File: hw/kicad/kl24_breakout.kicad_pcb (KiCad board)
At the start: 2 copper layers, 36.1 x 20.8 mm, 65 parts, among them J1 USB-micro-ab, J2 ARM_10PIN, P1 BATT+, P10 TST, P11 TST, P12 TST, P13 TST, P14 TST, P15 TST, P16 TST, P17 TST, P18 TST, P19 TST, P2 BATT-, P20 TST, P21 TST, P22 TST, P23 TST, P24 TST, P25 TST, P26 TST, P27 TST, P28 TST, P29 TST, P3 TST, P30 TST, P31 TST, P32 TST, P33 TST, P34 TST, P35 BATT_BACKUP+, P36 BATT_BACKUP-, P37 USB_V, P38 USB_GND, P4 TST, P5 TST, P6 TST, P7 TST, P8 TST, P9 TST, U1 MCP73831, U2 M25P05-A, U3 MKL24Z64VFM4, U4 MCP1640_SOT23, U5 LP3985, X1 CRYSTAL

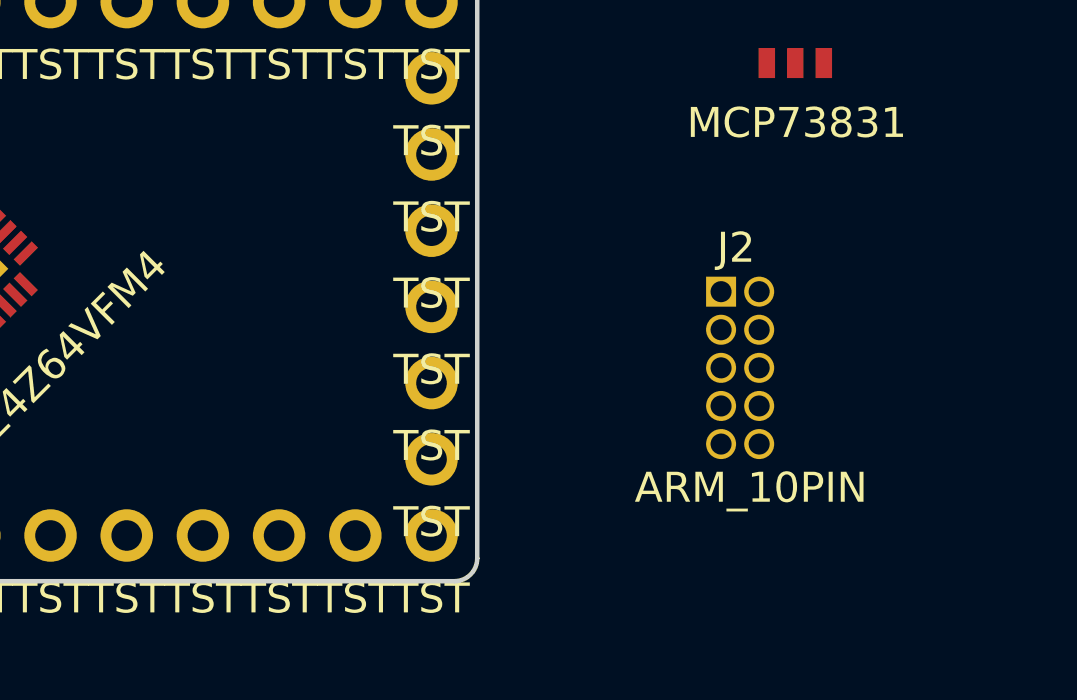
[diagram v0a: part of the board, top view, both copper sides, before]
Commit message: - switch arm 10pin header for smt version
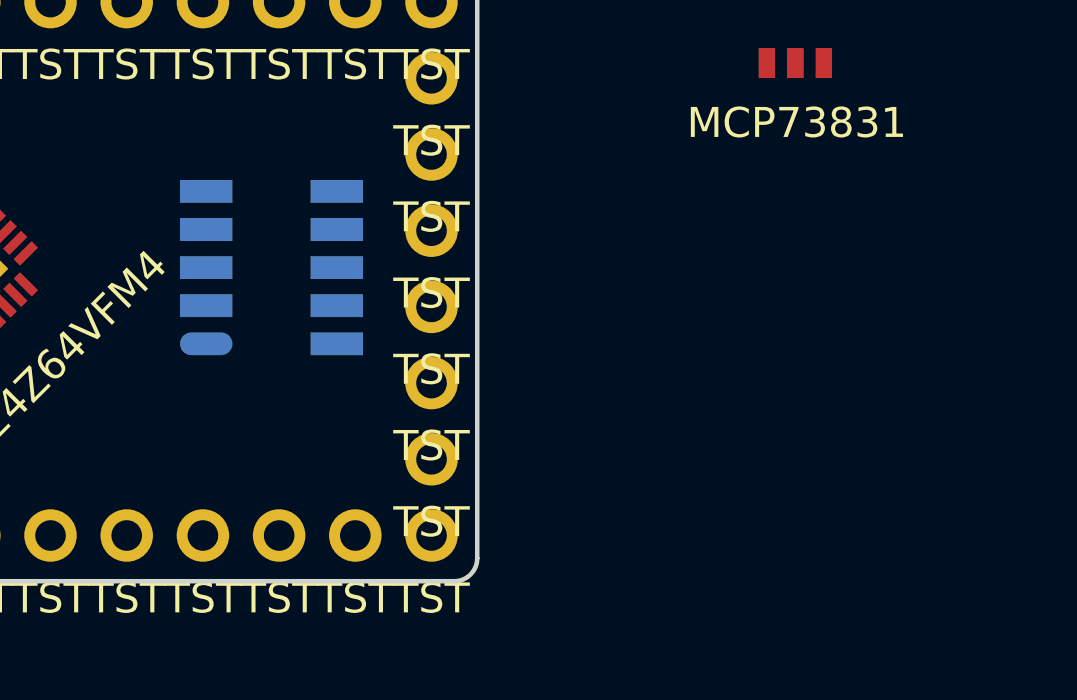
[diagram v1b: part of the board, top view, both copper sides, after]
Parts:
- J2: footprint ARM_10_PIN -> ARM_10_PIN_SMT; moved to B.Cu
- moved J2 15.3 mm to (139.4, 71.1), turned to 90 degrees
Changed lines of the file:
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@@
     (mod_text_size 1 1)
     (mod_text_width 0.15)
-    (pad_size 3.4 3.4)
-    (pad_drill 2)
+    (pad_size 0.76 1.75)
+    (pad_drill 0)
     (pad_to_mask_clearance 0)
     (aux_axis_origin 0 0)
-    (visible_elements FFFFFFBF)
+    (visible_elements 7FFFFFFF)
     (pcbplotparams
       (layerselection 3178497)
@@
     )
   )
-  (module ARM_10_PIN (layer F.Cu)
-    (at 154.432 74.422)
-    (fp_text reference J2 (at 0.5 -4) (layer F.SilkS)
-      (effects (font (size 1 1) (thickness 0.15)))
-    )
-    (fp_text value ARM_10PIN (at 1 4) (layer F.SilkS)
-      (effects (font (size 1 1) (thickness 0.15)))
-    )
-    (pad 1 thru_hole rect (at 0 -2.54) (size 1 1) (drill 0.70104)
-      (layers *.Cu *.Mask F.SilkS)
-      (net 24 3.3V_SUPPLY)
-    )
-    (pad 2 thru_hole circle (at 1.27 -2.54) (size 1 1) (drill 0.70104)
-      (layers *.Cu *.Mask F.SilkS)
-      (net 5 13)
-    )
-    (pad 3 thru_hole circle (at 0 -1.27) (size 1 1) (drill 0.70104)
-      (layers *.Cu *.Mask F.SilkS)
-      (net 12 2)
-    )
-    (pad 4 thru_hole circle (at 1.27 -1.27) (size 1 1) (drill 0.70104)
-      (layers *.Cu *.Mask F.SilkS)
-      (net 2 10)
-    )
-    (pad 5 thru_hole circle (at 0 0) (size 1 1) (drill 0.70104)
-      (layers *.Cu *.Mask F.SilkS)
-      (net 12 2)
-    )
-    (pad 6 thru_hole circle (at 1.27 0) (size 1 1) (drill 0.70104)
-      (layers *.Cu *.Mask F.SilkS)
-    )
-    (pad 7 thru_hole circle (at 0 1.27) (size 1 1) (drill 0.70104)
-      (layers *.Cu *.Mask F.SilkS)
-    )
-    (pad 8 thru_hole circle (at 1.27 1.27) (size 1 1) (drill 0.70104)
-      (layers *.Cu *.Mask F.SilkS)
-    )
-    (pad 9 thru_hole circle (at 0 2.54) (size 1 1) (drill 0.70104)
-      (layers *.Cu *.Mask F.SilkS)
-      (net 12 2)
-    )
-    (pad 10 thru_hole circle (at 1.27 2.54) (size 1 1) (drill 0.70104)
-      (layers *.Cu *.Mask F.SilkS)
-      (net 11 19)
-    )
-  )
   (module ABLS-8.000MHZ-B4-T (layer F.Cu)
     (at 118.11 97.79 180)
@@
     )
   )
+  (module ARM_10_PIN_SMT (layer B.Cu)
+    (at 139.446 71.12 90)
+    (fp_text reference J2 (at 0 4 90) (layer B.SilkS)
+      (effects (font (size 1 1) (thickness 0.15)) (justify mirror))
+    )
+    (fp_text value ARM_10PIN (at 0 -4 90) (layer B.SilkS)
+      (effects (font (size 1 1) (thickness 0.15)) (justify mirror))
+    )
+    (pad 1 smd oval (at -2.5 -2.175 90) (size 0.76 1.75)
+      (layers B.Cu B.Paste B.Mask)
+      (net 24 3.3V_SUPPLY)
+    )
+    (pad 2 smd rect (at -2.5 2.175 90) (size 0.76 1.75)
+      (layers B.Cu B.Paste B.Mask)
+      (net 5 13)
+    )
+    (pad 3 smd rect (at -1.23 -2.175 90) (size 0.76 1.75)
+      (layers B.Cu B.Paste B.Mask)
+      (net 12 2)
+    )
+    (pad 4 smd rect (at -1.23 2.175 90) (size 0.76 1.75)
+      (layers B.Cu B.Paste B.Mask)
+      (net 2 10)
+    )
+    (pad 5 smd rect (at 0.04 -2.175 90) (size 0.76 1.75)
+      (layers B.Cu B.Paste B.Mask)
+      (net 12 2)
+    )
+    (pad 6 smd rect (at 0.04 2.175 90) (size 0.76 1.75)
+      (layers B.Cu B.Paste B.Mask)
+    )
+    (pad 7 smd rect (at 1.31 -2.175 90) (size 0.76 1.75)
+      (layers B.Cu B.Paste B.Mask)
+    )
+    (pad 8 smd rect (at 1.31 2.175 90) (size 0.76 1.75)
+      (layers B.Cu B.Paste B.Mask)
+    )
+    (pad 9 smd rect (at 2.58 -2.175 90) (size 0.76 1.75)
+      (layers B.Cu B.Paste B.Mask)
+      (net 12 2)
+    )
+    (pad 10 smd rect (at 2.58 2.175 90) (size 0.76 1.75)
+      (layers B.Cu B.Paste B.Mask)
+      (net 11 19)
+    )
+  )

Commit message: - remove lv pwr supply
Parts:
- removed C8: 10uF, SM0603_Capa
- removed C9: 1uF, SM0603_Capa
- removed L1: INDUCTOR, SM1210
- removed P37: USB_V, TEST_0.100
- removed P38: USB_GND, TEST_0.100
- removed R5: 0R, SM0603_Resistor
- removed R6: 562K, SM0603_Resistor
- removed R7: 976K, SM0603_Resistor
- removed U5: LP3985, LP3985
- C4: value 22pF -> 1uF
- C5: value 4.7uF -> 1uF
- C6: value 1uF -> 22pF
- P3: value TST -> USB_V
- P35: value BATT_BACKUP+ -> TST
- P36: value BATT_BACKUP- -> TST
- P4: value TST -> USB_GND
- U4: value MCP1640_SOT23 -> LP3985
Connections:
- C4 pad 1: 17 -> USB_VBUS
- C5 pad 1: LV_SUPP_VIN -> 3.3V_SUPPLY
- C6 pad 1: USB_VBUS -> 17
- P10 pad 1: 2 -> 6
- P11 pad 1: 9 -> 3.3V_SUPPLY
- P12 pad 1: 10 -> 2
- P13 pad 1: 11 -> 9
- P14 pad 1: 12 -> 10
- P15 pad 1: 13 -> 11
- P16 pad 1: 14 -> 12
- P17 pad 1: 15 -> 13
- P18 pad 1: 16 -> 14
- P19 pad 1: 17 -> 15
- P20 pad 1: 18 -> 16
- P21 pad 1: 19 -> 17
- P22 pad 1: 20 -> 18
- P23 pad 1: 21 -> 19
- P24 pad 1: 22 -> 20
- P25 pad 1: 23 -> 21
- P26 pad 1: 24 -> 22
- P27 pad 1: 25 -> 23
- P28 pad 1: 26 -> 24
- P29 pad 1: 27 -> 25
- P3 pad 1: 1 -> USB_VBUS
- P30 pad 1: 28 -> 26
- P31 pad 1: 29 -> 27
- P32 pad 1: 30 -> 28
- P33 pad 1: 31 -> 29
- P34 pad 1: 32 -> 30
- P35 pad 1: LV_SUPP_VIN -> 31
- P36 pad 1: 2 -> 32
- P5 pad 1: 3 -> 1
- P6 pad 1: 4 -> 2
- P7 pad 1: 5 -> 3
- P8 pad 1: 6 -> 4
- P9 pad 1: 3.3V_SUPPLY -> 5
- U4 pad 1: N-0000049 -> USB_VBUS
- U4 pad 3: LV_SUPP_VIN -> USB_VBUS
- U4 pad 4: N-0000048 -> (no net)
- U4 pad 5: N-0000050 -> 3.3V_SUPPLY
- U4 pad 6: LV_SUPP_VIN -> (no net)

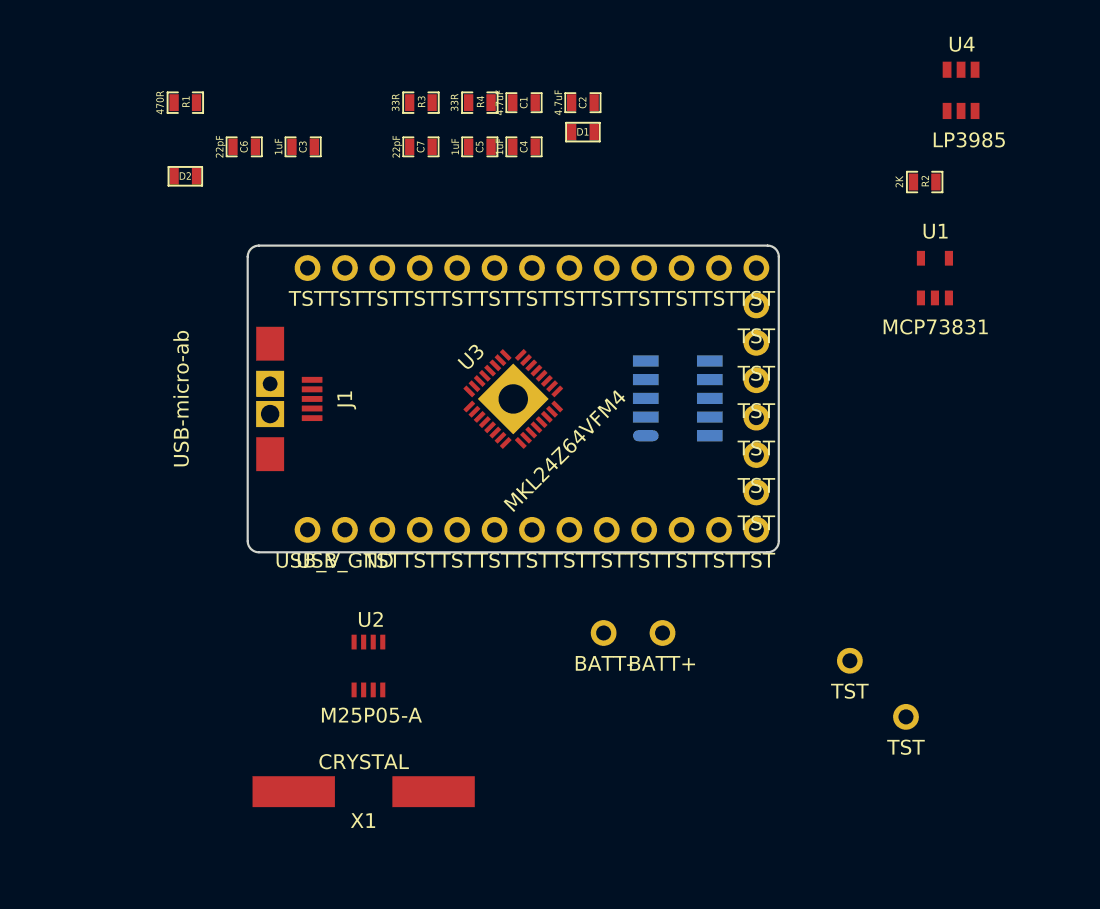
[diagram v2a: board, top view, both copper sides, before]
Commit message: - change to smt crystal
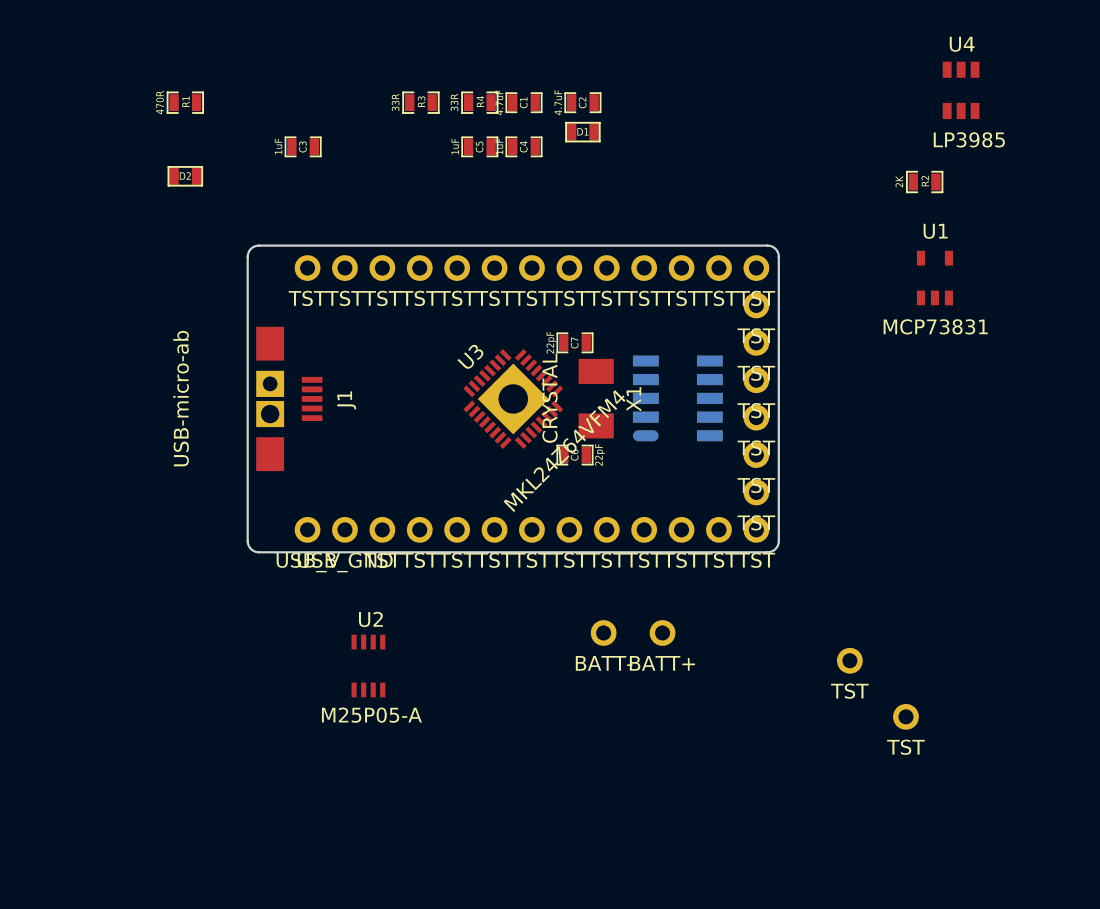
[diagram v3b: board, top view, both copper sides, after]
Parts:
- X1: footprint ABLS-8.000MHZ-B4-T -> XTAL_7A-8-000MAAE-T
- moved X1 31.0 mm to (133.9, 71.1), turned to 270 degrees
- moved C6 30.7 mm to (132.5, 74.9), turned to 180 degrees
- moved C7 16.9 mm to (132.5, 67.3)
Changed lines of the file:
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@@
-(kicad_pcb (version 3) (host pcbnew "(2013-03-31 BZR 4008)-stable")
+(kicad_pcb (version 3) (host pcbnew "(2013-03-04 BZR 3984)-stable")
   (general
     (links 88)
     (no_connects 88)
-    (area 103.65685 46.233 166.785222 101.034402)
+    (area 103.65685 46.233 162.896333 101.034402)
     (thickness 1.6)
     (drawings 8)
@@
     (mod_text_size 1 1)
     (mod_text_width 0.15)
-    (pad_size 0.76 1.75)
+    (pad_size 1.7 2.4)
     (pad_drill 0)
     (pad_to_mask_clearance 0)
@@
   )
   (module SM0603_Capa (layer F.Cu)
-    (at 110 54)
+    (at 132.461 74.93 180)
     (attr smd)
-    (fp_text reference C6 (at 0 0 90) (layer F.SilkS)
-      (effects (font (size 0.508 0.4572) (thickness 0.1143)))
-    )
-    (fp_text value 22pF (at -1.651 0 90) (layer F.SilkS)
+    (fp_text reference C6 (at 0 0 270) (layer F.SilkS)
+      (effects (font (size 0.508 0.4572) (thickness 0.1143)))
+    )
+    (fp_text value 22pF (at -1.651 0 270) (layer F.SilkS)
+      (effects (font (size 0.508 0.4572) (thickness 0.1143)))
+    )
+    (fp_line (start 0.50038 0.65024) (end 1.19888 0.65024) (layer F.SilkS) (width 0.11938))
+    (fp_line (start -0.50038 0.65024) (end -1.19888 0.65024) (layer F.SilkS) (width 0.11938))
+    (fp_line (start 0.50038 -0.65024) (end 1.19888 -0.65024) (layer F.SilkS) (width 0.11938))
+    (fp_line (start -1.19888 -0.65024) (end -0.50038 -0.65024) (layer F.SilkS) (width 0.11938))
+    (fp_line (start 1.19888 -0.635) (end 1.19888 0.635) (layer F.SilkS) (width 0.11938))
+    (fp_line (start -1.19888 0.635) (end -1.19888 -0.635) (layer F.SilkS) (width 0.11938))
+    (pad 1 smd rect (at -0.762 0 180) (size 0.635 1.143)
+      (layers F.Cu F.Paste F.Mask)
+      (net 9 17)
+    )
+    (pad 2 smd rect (at 0.762 0 180) (size 0.635 1.143)
+      (layers F.Cu F.Paste F.Mask)
+      (net 12 2)
+    )
+    (model smd\capacitors\C0603.wrl
+      (at (xyz 0 0 0.001))
+      (scale (xyz 0.5 0.5 0.5))
+      (rotate (xyz 0 0 0))
+    )
+  )
+  (module SM0603_Capa (layer F.Cu)
+    (at 114 54)
+    (attr smd)
+    (fp_text reference C3 (at 0 0 90) (layer F.SilkS)
+      (effects (font (size 0.508 0.4572) (thickness 0.1143)))
+    )
+    (fp_text value 1uF (at -1.651 0 90) (layer F.SilkS)
       (effects (font (size 0.508 0.4572) (thickness 0.1143)))
     )
@@
     (pad 1 smd rect (at -0.762 0) (size 0.635 1.143)
       (layers F.Cu F.Paste F.Mask)
-      (net 9 17)
+      (net 24 3.3V_SUPPLY)
     )
     (pad 2 smd rect (at 0.762 0) (size 0.635 1.143)
@@
   )
   (module SM0603_Capa (layer F.Cu)
-    (at 114 54)
+    (at 129 51)
     (attr smd)
-    (fp_text reference C3 (at 0 0 90) (layer F.SilkS)
-      (effects (font (size 0.508 0.4572) (thickness 0.1143)))
-    )
-    (fp_text value 1uF (at -1.651 0 90) (layer F.SilkS)
+    (fp_text reference C1 (at 0 0 90) (layer F.SilkS)
+      (effects (font (size 0.508 0.4572) (thickness 0.1143)))
+    )
+    (fp_text value 4.7uF (at -1.651 0 90) (layer F.SilkS)
       (effects (font (size 0.508 0.4572) (thickness 0.1143)))
     )
@@
     (pad 1 smd rect (at -0.762 0) (size 0.635 1.143)
       (layers F.Cu F.Paste F.Mask)
-      (net 24 3.3V_SUPPLY)
+      (net 38 USB_VBUS)
     )
     (pad 2 smd rect (at 0.762 0) (size 0.635 1.143)
@@
   )
   (module SM0603_Capa (layer F.Cu)
-    (at 129 51)
+    (at 132.461 67.31)
     (attr smd)
-    (fp_text reference C1 (at 0 0 90) (layer F.SilkS)
-      (effects (font (size 0.508 0.4572) (thickness 0.1143)))
-    )
-    (fp_text value 4.7uF (at -1.651 0 90) (layer F.SilkS)
+    (fp_text reference C7 (at 0 0 90) (layer F.SilkS)
+      (effects (font (size 0.508 0.4572) (thickness 0.1143)))
+    )
+    (fp_text value 22pF (at -1.651 0 90) (layer F.SilkS)
       (effects (font (size 0.508 0.4572) (thickness 0.1143)))
     )
@@
     (pad 1 smd rect (at -0.762 0) (size 0.635 1.143)
       (layers F.Cu F.Paste F.Mask)
-      (net 38 USB_VBUS)
+      (net 10 18)
     )
     (pad 2 smd rect (at 0.762 0) (size 0.635 1.143)
@@
   )
   (module SM0603_Capa (layer F.Cu)
-    (at 122 54)
+    (at 126 54)
     (attr smd)
-    (fp_text reference C7 (at 0 0 90) (layer F.SilkS)
-      (effects (font (size 0.508 0.4572) (thickness 0.1143)))
-    )
-    (fp_text value 22pF (at -1.651 0 90) (layer F.SilkS)
+    (fp_text reference C5 (at 0 0 90) (layer F.SilkS)
+      (effects (font (size 0.508 0.4572) (thickness 0.1143)))
+    )
+    (fp_text value 1uF (at -1.651 0 90) (layer F.SilkS)
       (effects (font (size 0.508 0.4572) (thickness 0.1143)))
     )
@@
     (pad 1 smd rect (at -0.762 0) (size 0.635 1.143)
       (layers F.Cu F.Paste F.Mask)
-      (net 10 18)
+      (net 24 3.3V_SUPPLY)
     )
     (pad 2 smd rect (at 0.762 0) (size 0.635 1.143)
@@
   )
   (module SM0603_Capa (layer F.Cu)
-    (at 126 54)
+    (at 129 54)
     (attr smd)
-    (fp_text reference C5 (at 0 0 90) (layer F.SilkS)
+    (fp_text reference C4 (at 0 0 90) (layer F.SilkS)
       (effects (font (size 0.508 0.4572) (thickness 0.1143)))
     )
@@
     (pad 1 smd rect (at -0.762 0) (size 0.635 1.143)
       (layers F.Cu F.Paste F.Mask)
-      (net 24 3.3V_SUPPLY)
-    )
-    (pad 2 smd rect (at 0.762 0) (size 0.635 1.143)
-      (layers F.Cu F.Paste F.Mask)
-      (net 12 2)
-    )
-    (model smd\capacitors\C0603.wrl
-      (at (xyz 0 0 0.001))
-      (scale (xyz 0.5 0.5 0.5))
-      (rotate (xyz 0 0 0))
-    )
-  )
-  (module SM0603_Capa (layer F.Cu)
-    (at 129 54)
-    (attr smd)
-    (fp_text reference C4 (at 0 0 90) (layer F.SilkS)
-      (effects (font (size 0.508 0.4572) (thickness 0.1143)))
-    )
-    (fp_text value 1uF (at -1.651 0 90) (layer F.SilkS)
-      (effects (font (size 0.508 0.4572) (thickness 0.1143)))
-    )
-    (fp_line (start 0.50038 0.65024) (end 1.19888 0.65024) (layer F.SilkS) (width 0.11938))
-    (fp_line (start -0.50038 0.65024) (end -1.19888 0.65024) (layer F.SilkS) (width 0.11938))
-    (fp_line (start 0.50038 -0.65024) (end 1.19888 -0.65024) (layer F.SilkS) (width 0.11938))
-    (fp_line (start -1.19888 -0.65024) (end -0.50038 -0.65024) (layer F.SilkS) (width 0.11938))
-    (fp_line (start 1.19888 -0.635) (end 1.19888 0.635) (layer F.SilkS) (width 0.11938))
-    (fp_line (start -1.19888 0.635) (end -1.19888 -0.635) (layer F.SilkS) (width 0.11938))
-    (pad 1 smd rect (at -0.762 0) (size 0.635 1.143)
-      (layers F.Cu F.Paste F.Mask)
       (net 38 USB_VBUS)
     )
@@
     )
   )
-  (module ABLS-8.000MHZ-B4-T (layer F.Cu)
-    (at 118.11 97.79 180)
-    (fp_text reference X1 (at 0 -2 180) (layer F.SilkS)
-      (effects (font (size 1 1) (thickness 0.15)))
-    )
-    (fp_text value CRYSTAL (at 0 2 180) (layer F.SilkS)
-      (effects (font (size 1 1) (thickness 0.15)))
-    )
-    (pad 1 smd rect (at -4.75 0 180) (size 5.6 2.1)
-      (layers F.Cu F.Paste F.Mask)
-      (net 10 18)
-    )
-    (pad 2 smd rect (at 4.75 0 180) (size 5.6 2.1)
-      (layers F.Cu F.Paste F.Mask)
-      (net 9 17)
-    )
-  )
   (module ARM_10_PIN_SMT (layer B.Cu)
     (at 139.446 71.12 90)
@@
     )
   )
+  (module XTAL_7A-8-000MAAE-T (layer F.Cu)
+    (at 133.9 71.1 270)
+    (fp_text reference X1 (at 0 -2.6 270) (layer F.SilkS)
+      (effects (font (size 1 1) (thickness 0.15)))
+    )
+    (fp_text value CRYSTAL (at 0 3.1 270) (layer F.SilkS)
+      (effects (font (size 1 1) (thickness 0.15)))
+    )
+    (pad 1 smd rect (at -1.85 0 270) (size 1.7 2.4)
+      (layers F.Cu F.Paste F.Mask)
+      (net 10 18)
+    )
+    (pad 2 smd rect (at 1.85 0 270) (size 1.7 2.4)
+      (layers F.Cu F.Paste F.Mask)
+      (net 9 17)
+    )
+  )

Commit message: - redo micro ab connector footprint
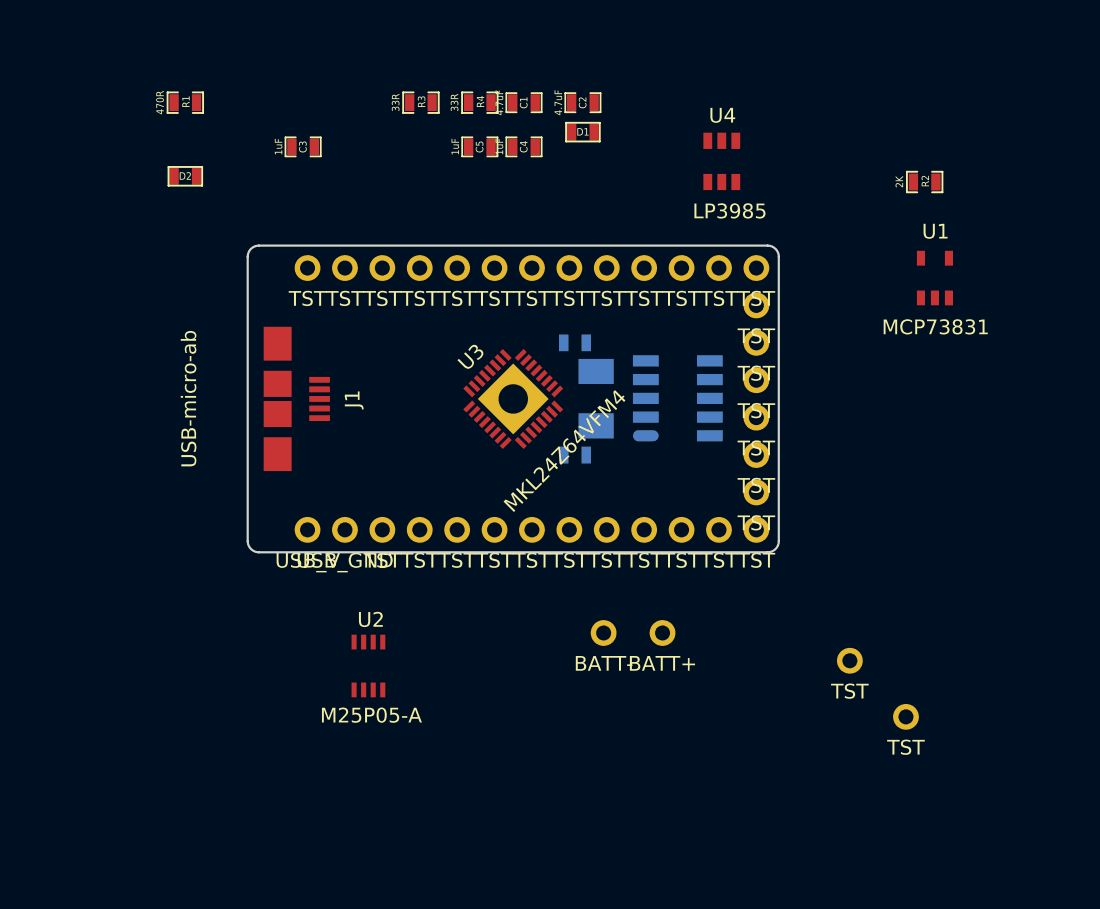
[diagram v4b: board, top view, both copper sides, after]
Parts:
- C6, C7, X1: moved to B.Cu
- moved U4 17.0 mm to (141.5, 56.4)
- moved J1 0.51 mm to (112.3, 71.1)
- turned X1 to 90 degrees
